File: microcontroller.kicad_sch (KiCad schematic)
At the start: 43 parts, among them J5 USB4105-GF-A, J6 LEFT, J7 DEBUG, J8 RIGHT, U2 W25Q32JV, U3 RP2350A, U4 MCP1702T-3302E_CB, X1 IQXO-791

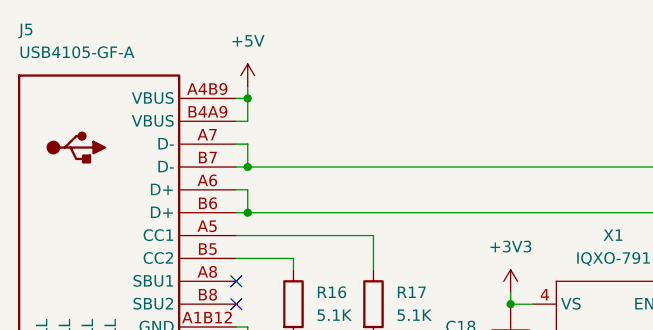
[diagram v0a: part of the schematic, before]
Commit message: Add nixie tube net labels and dc/dc converter
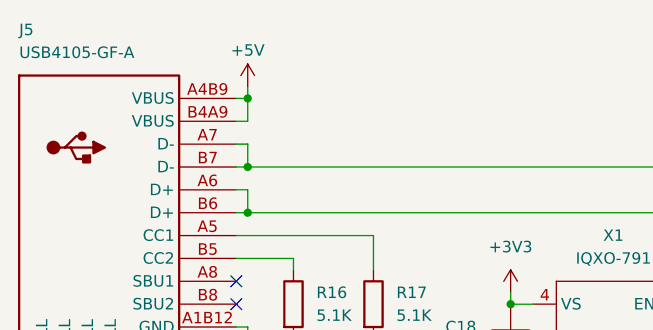
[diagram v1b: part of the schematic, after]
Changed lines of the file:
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@@
 		(on_board yes)
 		(dnp no)
-		(fields_autoplaced yes)
 		(property "Reference" "#PWR029"
 			(at 39.37 21.59 0)
@@
 		)
 		(property "Value" "+5V"
-			(at 39.37 12.7 0)
+			(at 39.37 13.716 0)
 			(effects
 				(font

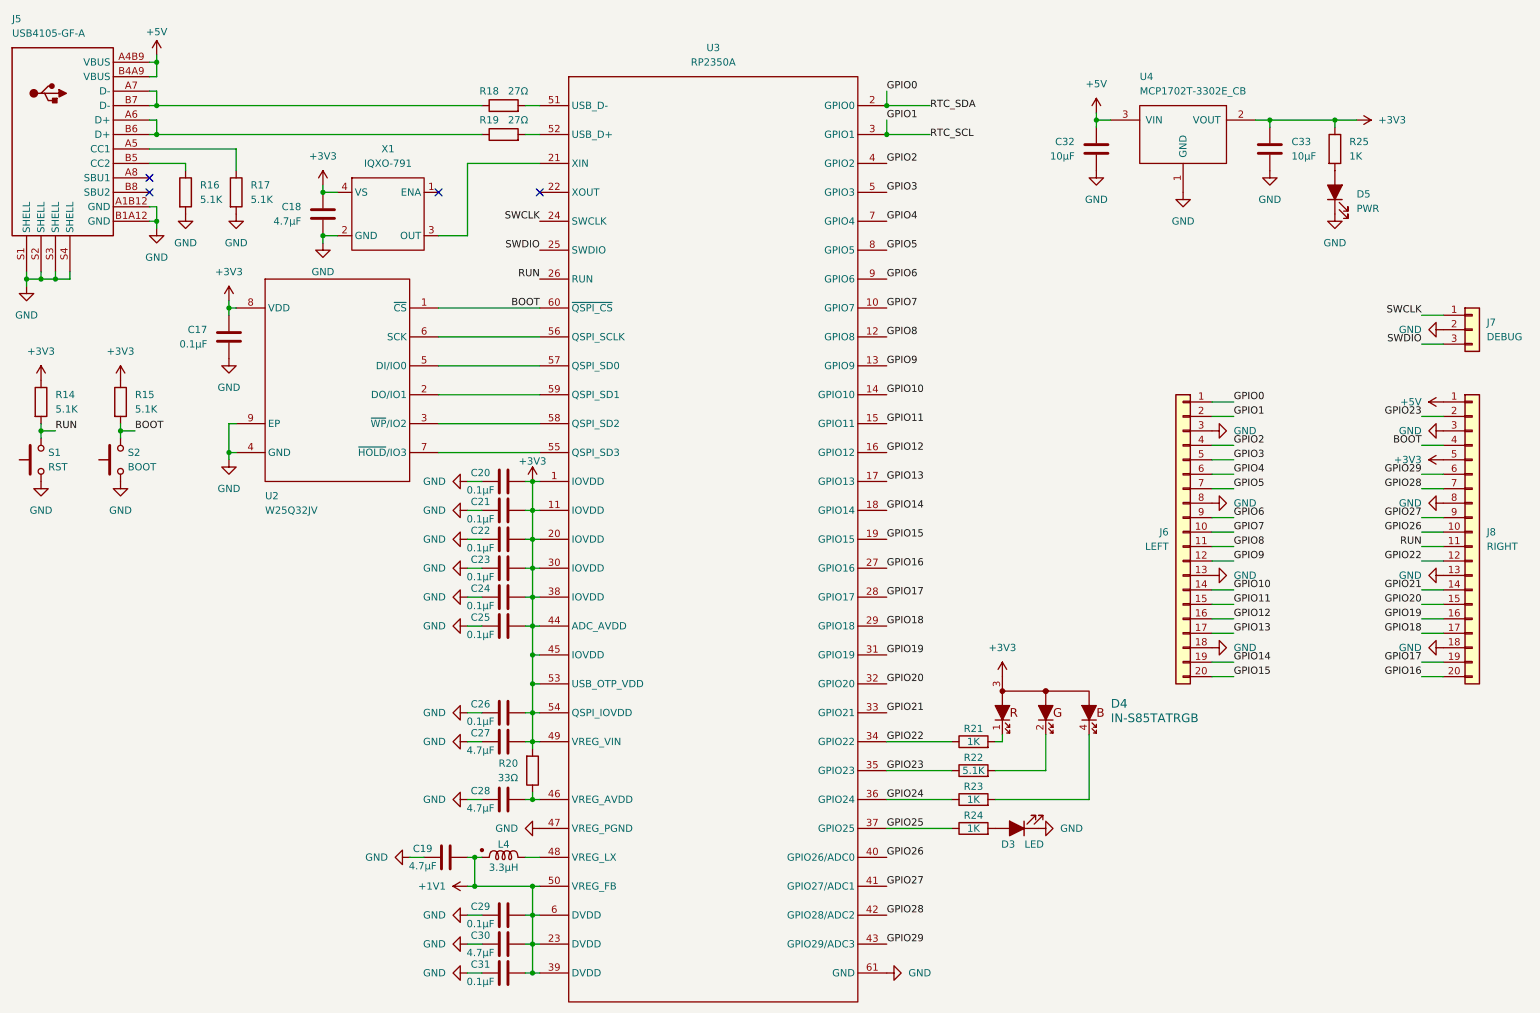
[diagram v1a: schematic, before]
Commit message: Add 12V boost converter
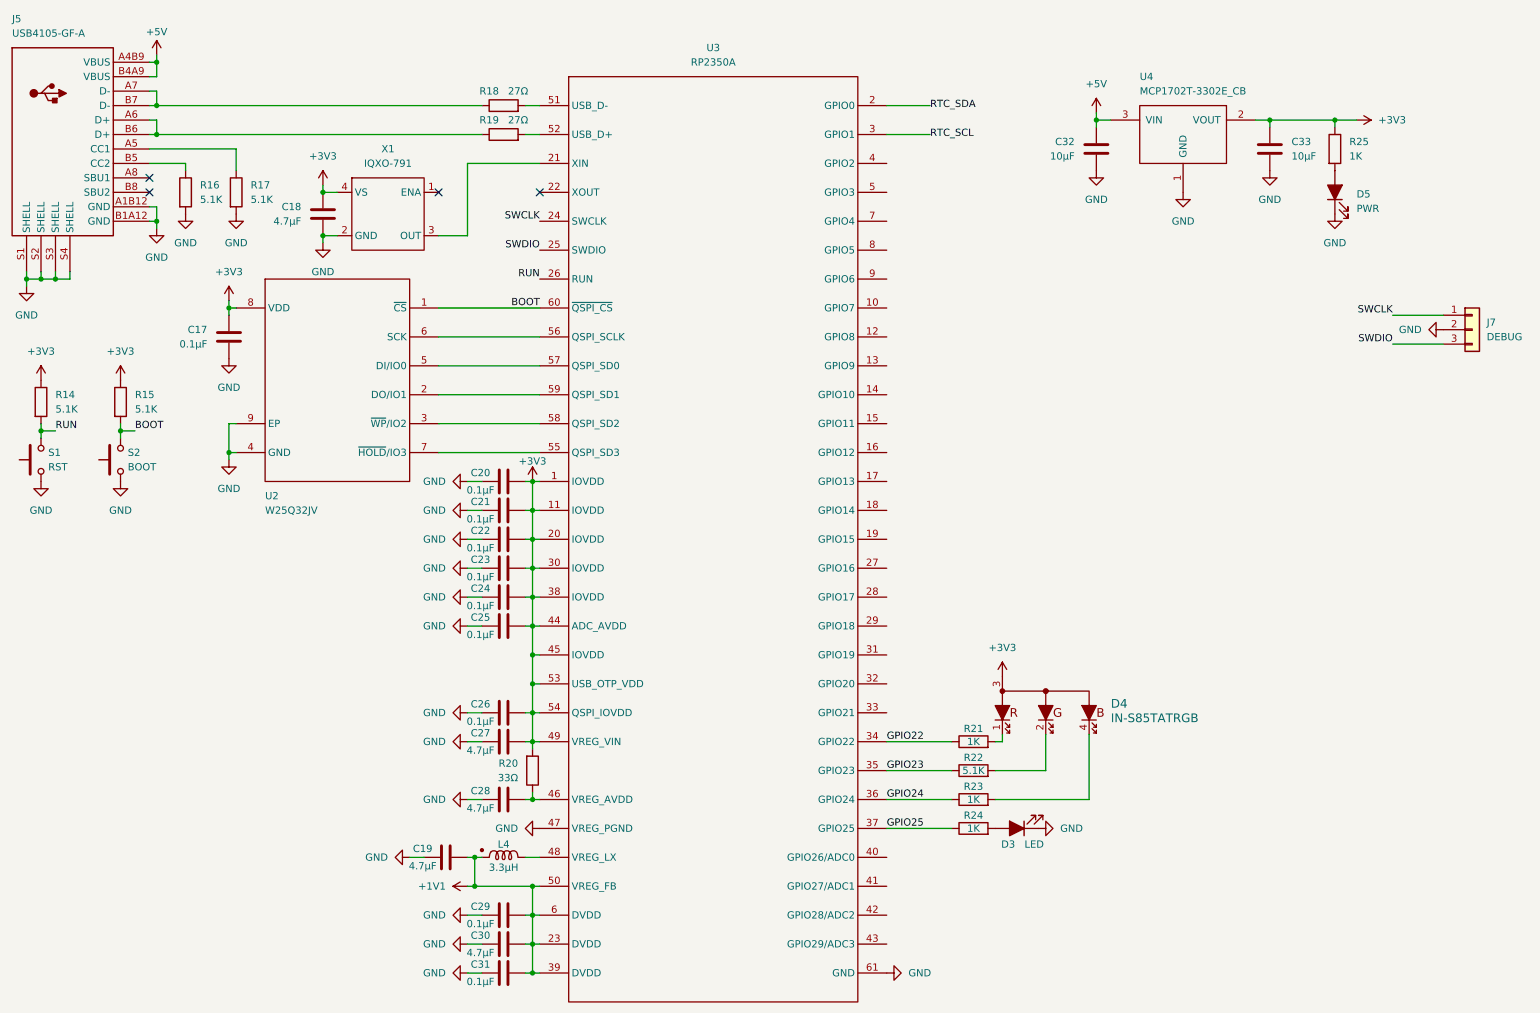
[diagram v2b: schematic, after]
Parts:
- removed J6: LEFT, Connector_PinHeader_2.54mm:PinHeader_1x20_P2.54mm_Vertical, symbol Connector_Generic:Conn_01x20
- removed J8: RIGHT, Connector_PinHeader_2.54mm:PinHeader_1x20_P2.54mm_Vertical, symbol Connector_Generic:Conn_01x20
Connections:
- net GPIO0 renamed RTC_SDA
- net GPIO1 renamed RTC_SCL
- net GPIO10: no longer names the net of U3.14 (GPIO10)
- net GPIO11: no longer names the net of U3.15 (GPIO11)
- net GPIO12: no longer names the net of U3.16 (GPIO12)
- net GPIO13: no longer names the net of U3.17 (GPIO13)
- net GPIO14: no longer names the net of U3.18 (GPIO14)
- net GPIO15: no longer names the net of U3.19 (GPIO15)
- net GPIO16: no longer names the net of U3.27 (GPIO16)
- net GPIO17: no longer names the net of U3.28 (GPIO17)
- net GPIO18: no longer names the net of U3.29 (GPIO18)
- net GPIO19: no longer names the net of U3.31 (GPIO19)
- net GPIO2: no longer names the net of U3.4 (GPIO2)
- net GPIO20: no longer names the net of U3.32 (GPIO20)
- net GPIO21: no longer names the net of U3.33 (GPIO21)
- net GPIO26: no longer names the net of U3.40 (GPIO26/ADC0)
- net GPIO27: no longer names the net of U3.41 (GPIO27/ADC1)
- net GPIO28: no longer names the net of U3.42 (GPIO28/ADC2)
- net GPIO29: no longer names the net of U3.43 (GPIO29/ADC3)
- net GPIO3: no longer names the net of U3.5 (GPIO3)
- net GPIO4: no longer names the net of U3.7 (GPIO4)
- net GPIO5: no longer names the net of U3.8 (GPIO5)
- net GPIO6: no longer names the net of U3.9 (GPIO6)
- net GPIO7: no longer names the net of U3.10 (GPIO7)
- net GPIO8: no longer names the net of U3.12 (GPIO8)
- net GPIO9: no longer names the net of U3.13 (GPIO9)

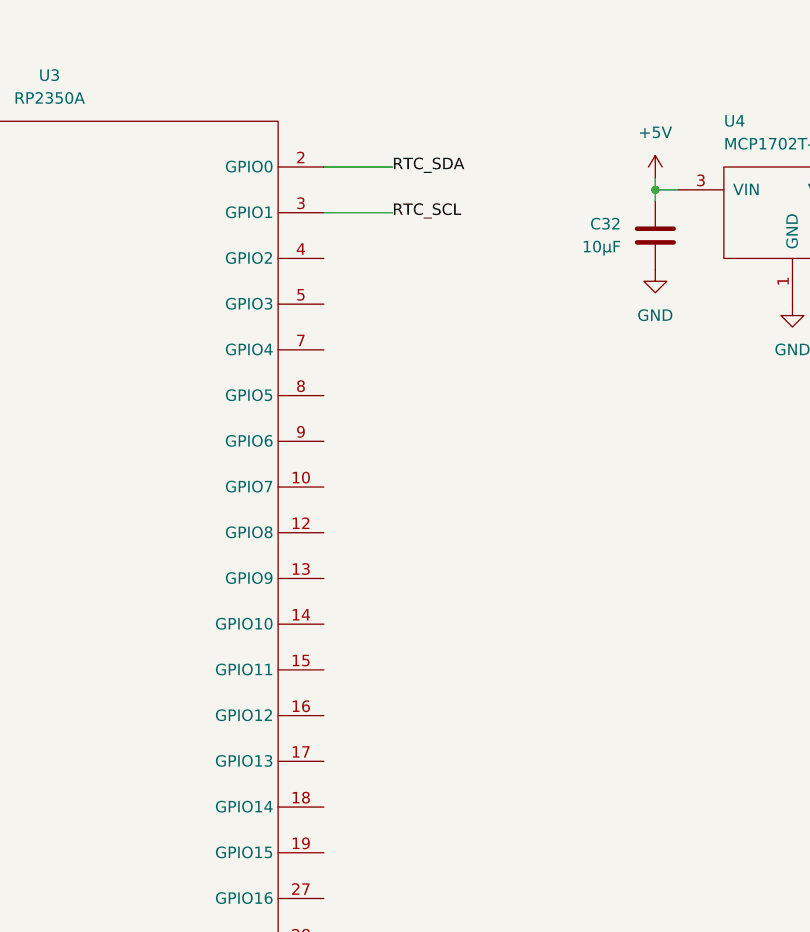
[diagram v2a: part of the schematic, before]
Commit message: Add data connections between driver and rp2350
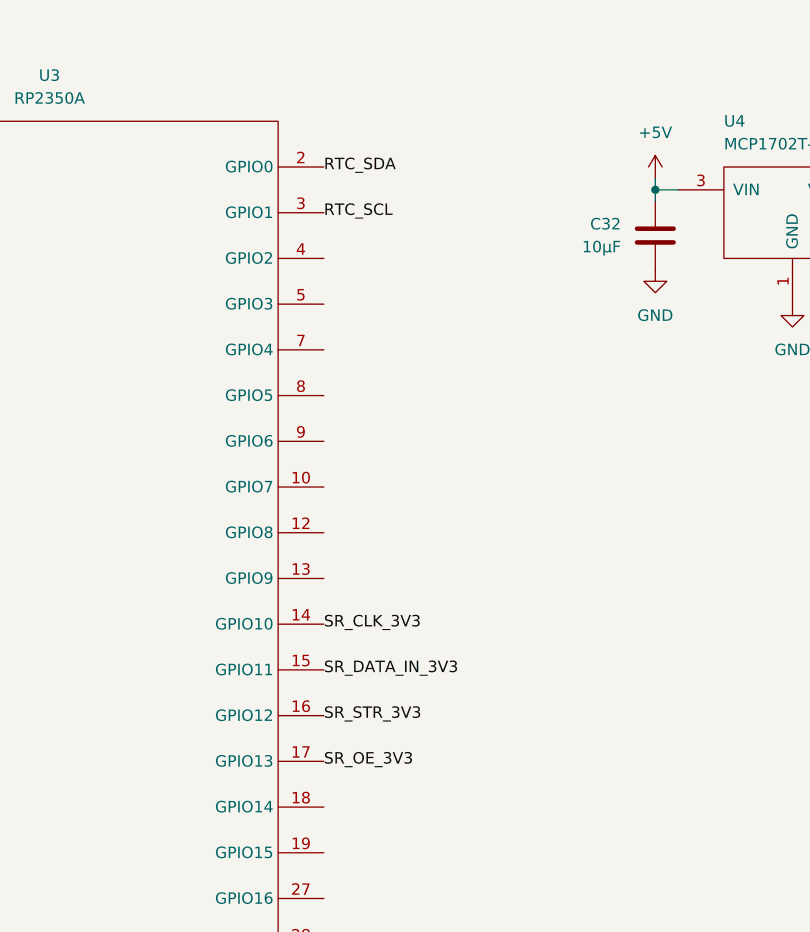
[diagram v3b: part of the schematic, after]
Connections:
- net SR_CLK_3V3: now reaches U3.14 (GPIO10)
- net SR_DATA_IN_3V3: now reaches U3.15 (GPIO11)
- net SR_STR_3V3: now reaches U3.16 (GPIO12)
- net SR_OE_3V3: now reaches U3.17 (GPIO13)
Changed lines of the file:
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@@
-	(wire
-		(pts
-			(xy 167.64 31.75) (xy 175.26 31.75)
-		)
-		(stroke
-			(width 0)
-			(type default)
-		)
-	)
 	(wire
 		(pts
@@
 		(pts
 			(xy 39.37 21.59) (xy 38.1 21.59)
-		)
-		(stroke
-			(width 0)
-			(type default)
-		)
-	)
-	(wire
-		(pts
-			(xy 167.64 26.67) (xy 175.26 26.67)
 		)
 		(stroke
@@
 		)
 	)
+	(label "SR_STR_3V3"
+		(at 167.64 87.63 0)
+		(effects
+			(font
+				(size 1.27 1.27)
+			)
+			(justify left)
+		)
+	)
 	(label "RTC_SCL"
-		(at 175.26 31.75 0)
+		(at 167.64 31.75 0)
 		(effects
 			(font
@@
 	)
 	(label "RTC_SDA"
-		(at 175.26 26.67 0)
+		(at 167.64 26.67 0)
+		(effects
+			(font
+				(size 1.27 1.27)
+			)
+			(justify left)
+		)
+	)
+	(label "SR_DATA_IN_3V3"
+		(at 167.64 82.55 0)
 		(effects
 			(font
@@
 		)
 	)
+	(label "SR_CLK_3V3"
+		(at 167.64 77.47 0)
+		(effects
+			(font
+				(size 1.27 1.27)
+			)
+			(justify left)
+		)
+	)
+	(label "SR_OE_3V3"
+		(at 167.64 92.71 0)
+		(effects
+			(font
+				(size 1.27 1.27)
+			)
+			(justify left)
+		)
+	)

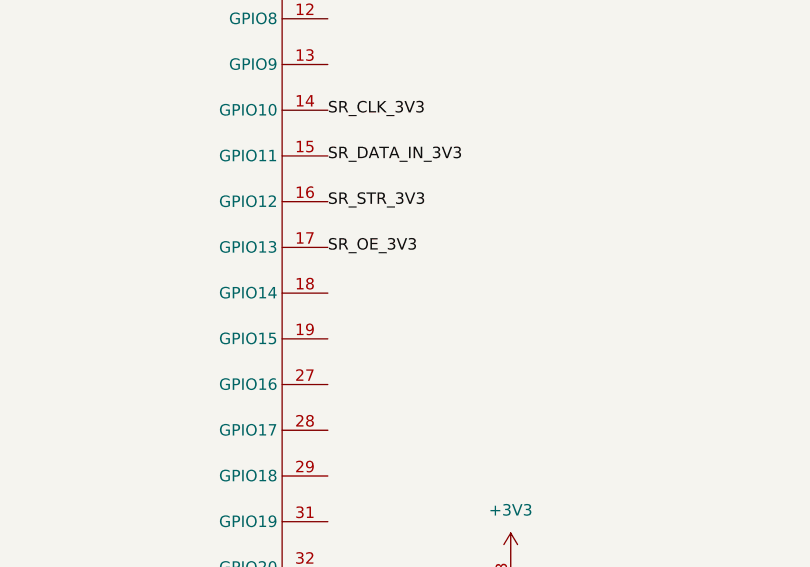
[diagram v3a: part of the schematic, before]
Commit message: Add backlight LEDs
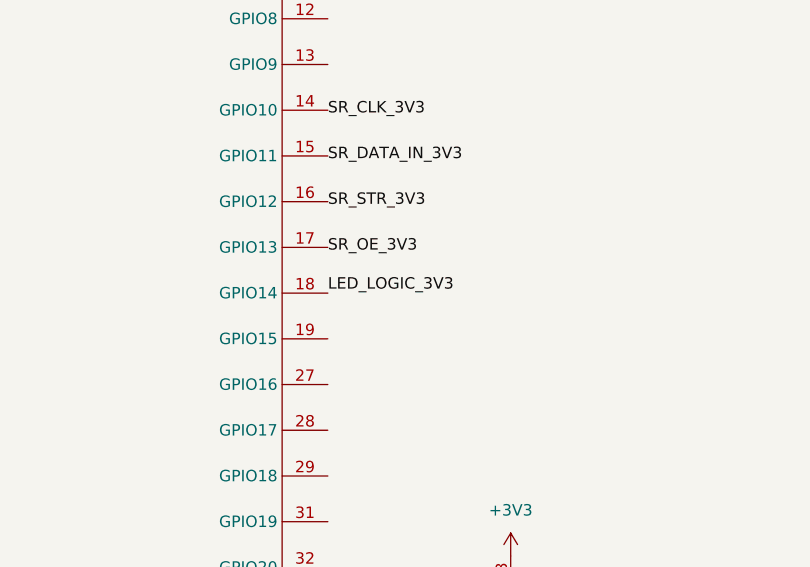
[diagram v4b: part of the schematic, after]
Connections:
- net LED_LOGIC_3V3: now reaches U3.18 (GPIO14)
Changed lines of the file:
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@@
+		)
+	)
+	(label "LED_LOGIC_3V3"
+		(at 167.64 97.79 0)
+		(effects
+			(font
+				(size 1.27 1.27)
+			)
+			(justify left bottom)
 		)
 	)

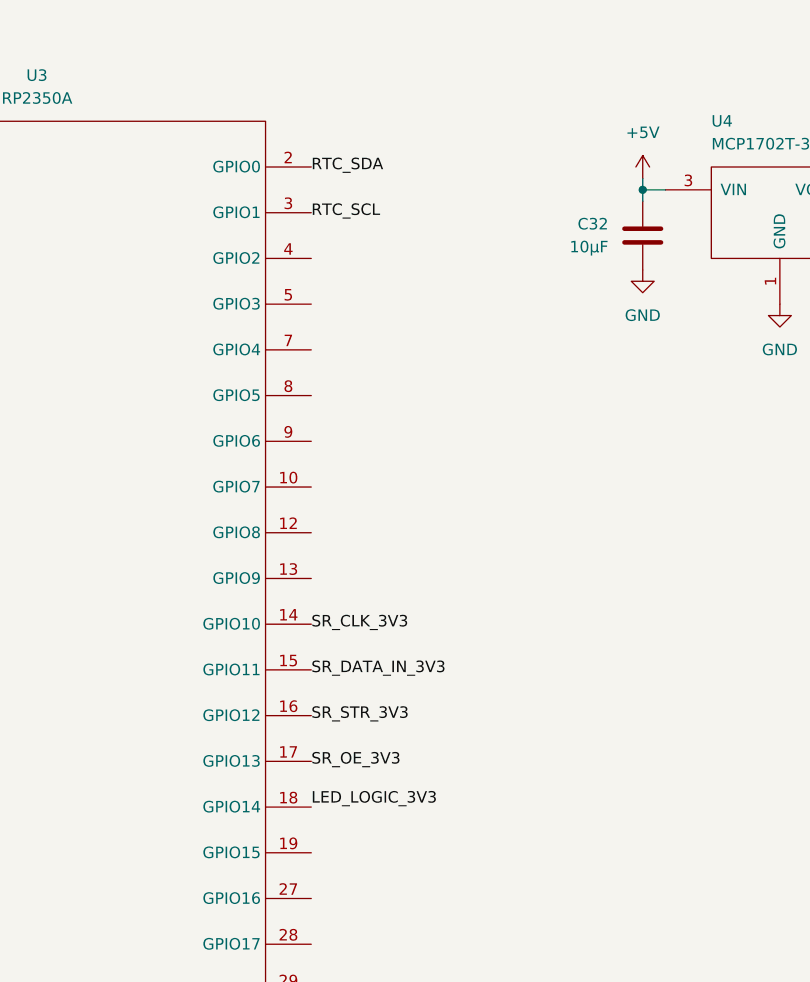
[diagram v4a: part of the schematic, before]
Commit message: Add global labels for nets spanning several sheets
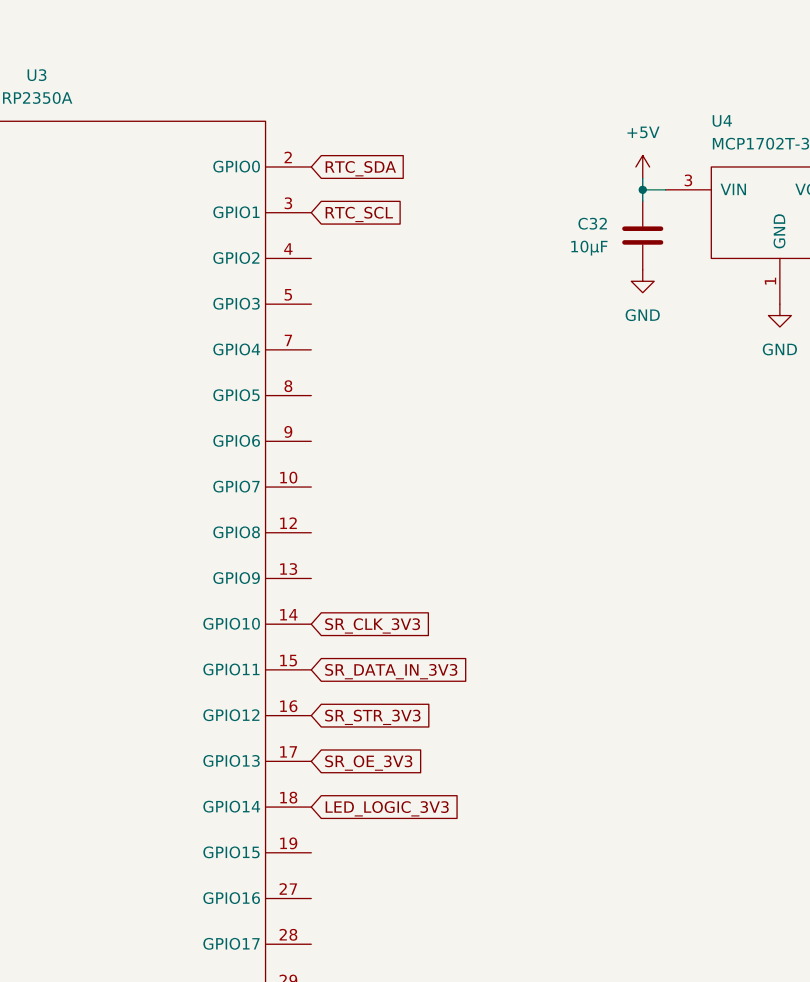
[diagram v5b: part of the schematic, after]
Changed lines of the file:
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@@
-		)
-	)
-	(label "SR_STR_3V3"
-		(at 167.64 87.63 0)
-		(effects
-			(font
-				(size 1.27 1.27)
-			)
-			(justify left)
-		)
-	)
-	(label "LED_LOGIC_3V3"
-		(at 167.64 97.79 0)
-		(effects
-			(font
-				(size 1.27 1.27)
-			)
-			(justify left bottom)
-		)
-	)
-	(label "RTC_SCL"
-		(at 167.64 31.75 0)
-		(effects
-			(font
-				(size 1.27 1.27)
-			)
-			(justify left)
-		)
-	)
-	(label "RTC_SDA"
-		(at 167.64 26.67 0)
-		(effects
-			(font
-				(size 1.27 1.27)
-			)
-			(justify left)
-		)
-	)
-	(label "SR_DATA_IN_3V3"
-		(at 167.64 82.55 0)
-		(effects
-			(font
-				(size 1.27 1.27)
-			)
-			(justify left)
 		)
 	)
@@
 		)
 	)
-	(label "SR_CLK_3V3"
-		(at 167.64 77.47 0)
-		(effects
-			(font
-				(size 1.27 1.27)
-			)
-			(justify left)
-		)
-	)
-	(label "SR_OE_3V3"
-		(at 167.64 92.71 0)
-		(effects
-			(font
-				(size 1.27 1.27)
-			)
-			(justify left)
-		)
-	)
 	(label "RUN"
 		(at 106.68 57.15 180)
@@
 		)
 	)
+	(global_label "SR_CLK_3V3"
+		(shape input)
+		(at 167.64 77.47 0)
+		(fields_autoplaced yes)
+		(effects
+			(font
+				(size 1.27 1.27)
+			)
+			(justify left)
+		)
+		(property "Intersheetrefs" "${INTERSHEET_REFS}"
+			(at 182.1156 77.47 0)
+			(effects
+				(font
+					(size 1.27 1.27)
+				)
+				(justify left)
+				(hide yes)
+			)
+		)
+	)
+	(global_label "RTC_SCL"
+		(shape input)
+		(at 167.64 31.75 0)
+		(fields_autoplaced yes)
+		(effects
+			(font
+				(size 1.27 1.27)
+			)
+			(justify left)
+		)
+		(property "Intersheetrefs" "${INTERSHEET_REFS}"
+			(at 178.608 31.75 0)
+			(effects
+				(font
+					(size 1.27 1.27)
+				)
+				(justify left)
+				(hide yes)
+			)
+		)
+	)
+	(global_label "SR_OE_3V3"
+		(shape input)
+		(at 167.64 92.71 0)
+		(fields_autoplaced yes)
+		(effects
+			(font
+				(size 1.27 1.27)
+			)
+			(justify left)
+		)
+		(property "Intersheetrefs" "${INTERSHEET_REFS}"
+			(at 181.027 92.71 0)
+			(effects
+				(font
+					(size 1.27 1.27)
+				)
+				(justify left)
+				(hide yes)
+			)
+		)
+	)
+	(global_label "SR_STR_3V3"
+		(shape input)
+		(at 167.64 87.63 0)
+		(fields_autoplaced yes)
+		(effects
+			(font
+				(size 1.27 1.27)
+			)
+			(justify left)
+		)
+		(property "Intersheetrefs" "${INTERSHEET_REFS}"
+			(at 181.9946 87.63 0)
+			(effects
+				(font
+					(size 1.27 1.27)
+				)
+				(justify left)
+				(hide yes)
+			)
+		)
+	)
+	(global_label "RTC_SDA"
+		(shape input)
+		(at 167.64 26.67 0)
+		(fields_autoplaced yes)
+		(effects
+			(font
+				(size 1.27 1.27)
+			)
+			(justify left)
+		)
+		(property "Intersheetrefs" "${INTERSHEET_REFS}"
+			(at 178.6685 26.67 0)
+			(effects
+				(font
+					(size 1.27 1.27)
+				)
+				(justify left)
+				(hide yes)
+			)
+		)
+	)
+	(global_label "SR_DATA_IN_3V3"
+		(shape input)
+		(at 167.64 82.55 0)
+		(fields_autoplaced yes)
+		(effects
+			(font
+				(size 1.27 1.27)
+			)
+			(justify left)
+		)
+		(property "Intersheetrefs" "${INTERSHEET_REFS}"
+			(at 185.8652 82.55 0)
+			(effects
+				(font
+					(size 1.27 1.27)
+				)
+				(justify left)
+				(hide yes)
+			)
+		)
+	)
+	(global_label "LED_LOGIC_3V3"
+		(shape input)
+		(at 167.64 97.79 0)
+		(fields_autoplaced yes)
+		(effects
+			(font
+				(size 1.27 1.27)
+			)
+			(justify left)
+		)
+		(property "Intersheetrefs" "${INTERSHEET_REFS}"
+			(at 185.0185 97.79 0)
+			(effects
+				(font
+					(size 1.27 1.27)
+				)
+				(justify left)
+				(hide yes)
+			)
+		)
+	)
